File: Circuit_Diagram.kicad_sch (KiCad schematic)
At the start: 2 parts

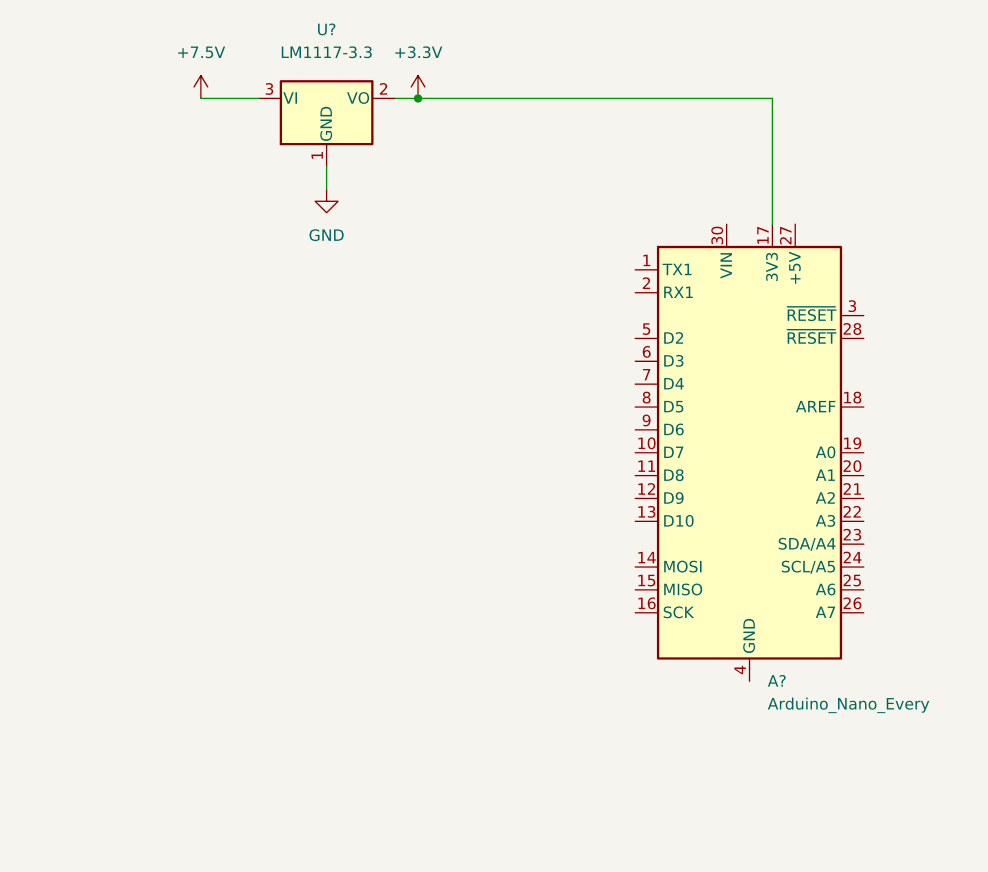
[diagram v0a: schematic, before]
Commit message: Update to add wifi module
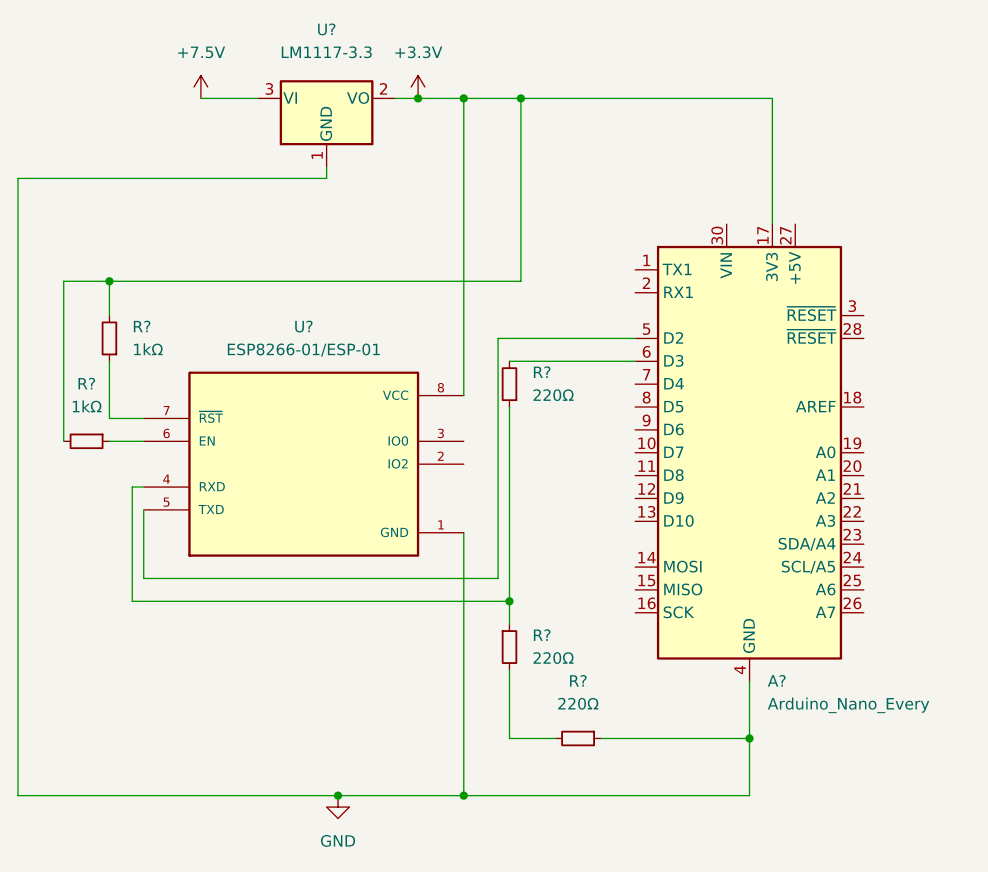
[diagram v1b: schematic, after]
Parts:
- added R? (x3): 220Ω, symbol Device:R_Small
- added R? (x2): 1kΩ, symbol Device:R_Small
- added U?: ESP8266-01/ESP-01, XCVR_ESP8266-01/ESP-01, symbol ESP8266:ESP8266-01/ESP-01
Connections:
- net +3V3: now also R?.2, R?.2, U?.8 (VCC)
- net GND: now also A?.29 (GND), A?.4 (GND), R?.1, U?.1 (GND)
- net at A?.5 (D2): now also U?.5 (TXD)
- net at A?.6 (D3): now also R?.2
- new net: R?.1, R?.1, U?.4 (RXD)
- new net: R?.1, U?.7 (~{RST})
- new net: R?.2, R?.2
- new net: R?.1, U?.6 (EN)
